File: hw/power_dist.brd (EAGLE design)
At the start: 80 x 50 mm, 72 parts, among them J1 JST-ZH6SMT_VERT, J2 JST-PH4SMT_VERT, J3 JST-PH5VERT, P1 XT30P, P2 XT30P, P3 XT30P, P4 XT30P, P5 XT30P, P6 XT30P, P7 XT90PW-M, Q1 PSMN4R8-100BSEJ, Q2 PSMN4R8-100BSEJ, Q3 PSMN4R8-100BSEJ, Q4 MF-DSC-SOT233-MMBT3904, Q5 MMBT5401 100V, U1 MAX15062AATA+T, U2 STM32G474CEU6, U4 TCAN334G, U5 LT1787HVIMS8PBF

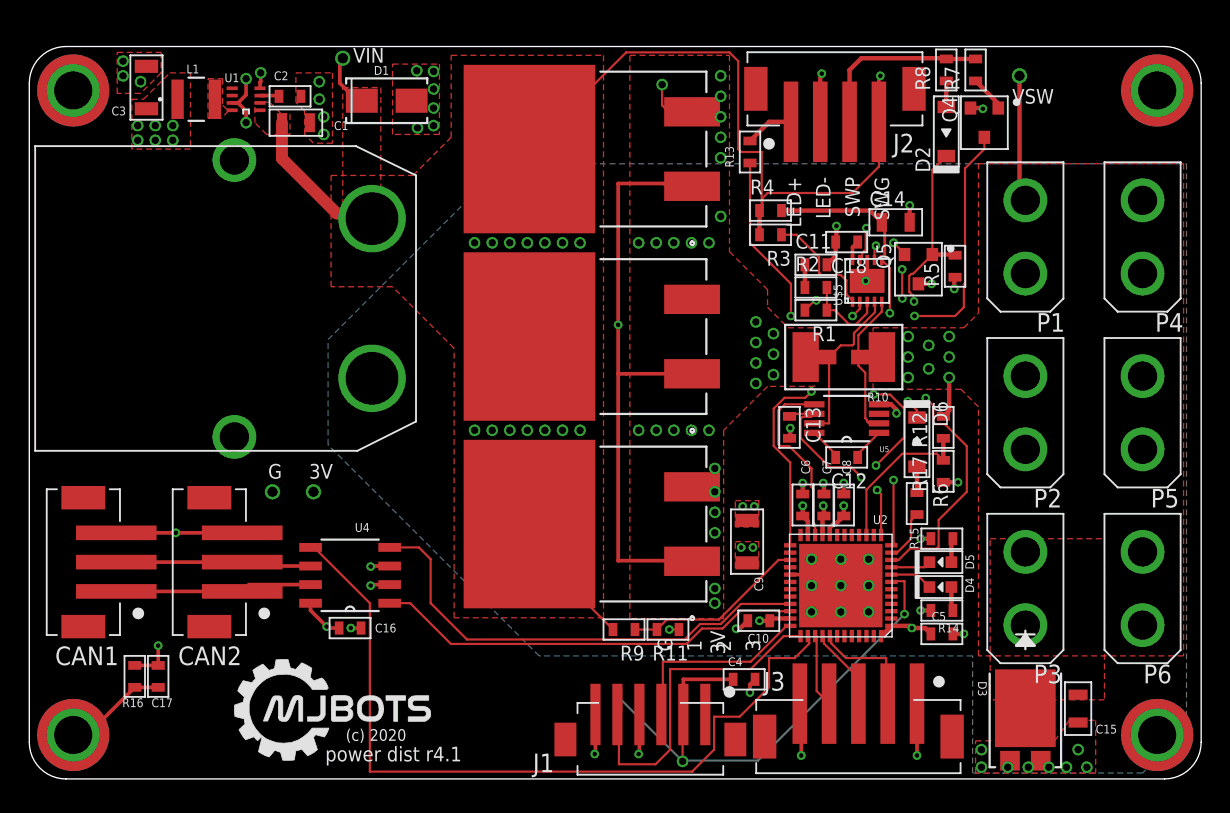
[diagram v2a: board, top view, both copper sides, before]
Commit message: Connect GND/PGND and fix XT90 TH size
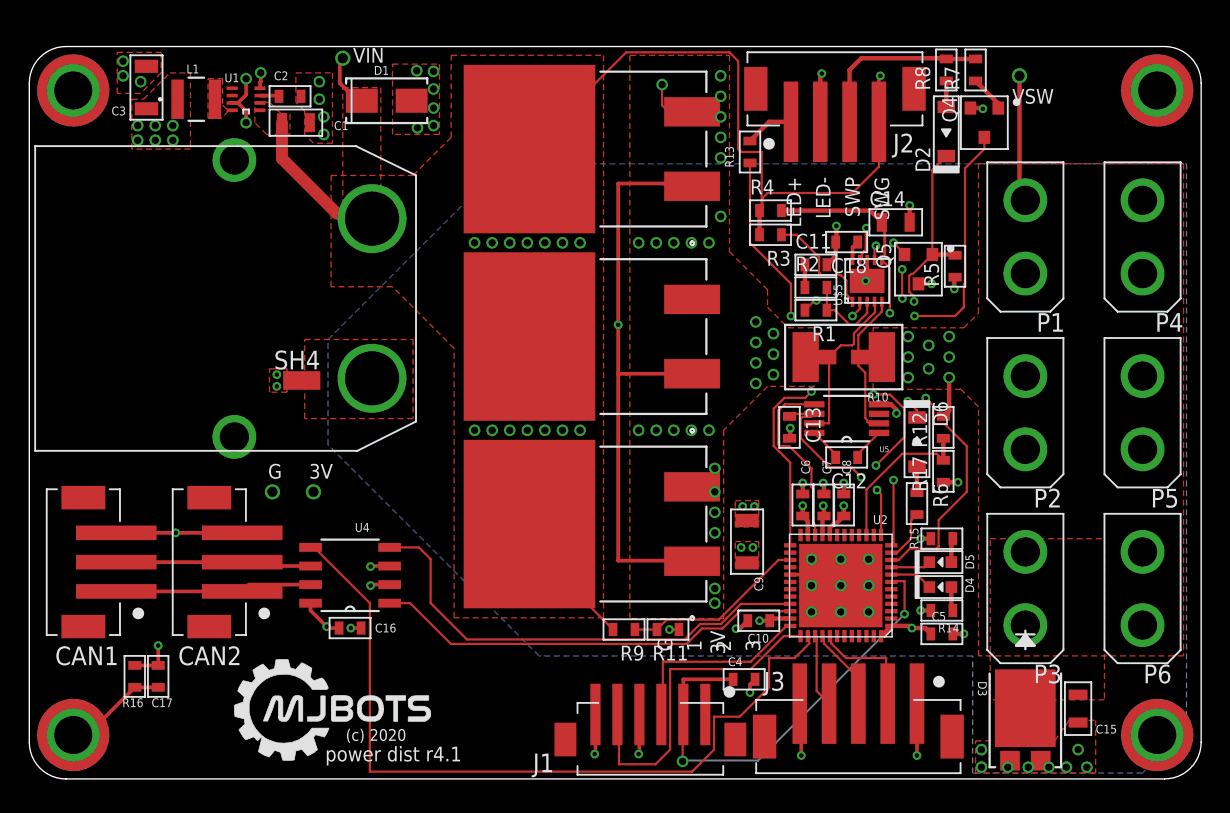
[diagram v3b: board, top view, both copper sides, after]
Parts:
- added SH4: SHORTBIG, shorts:SHORT_TOP-BIG
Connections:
- net GND: now also SH4.1
- net PGND: now also SH4.2
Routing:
- net NRST: track 37.7 -> 31.5 mm
- net GPIO3: track 10.4 -> 7.91 mm
- net SWCLK: track 24.7 -> 22.7 mm
- net GND: vias 49 -> 51
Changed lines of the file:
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@@
 </element>
 <element name="U4" library="precharge" package="SOIC8" value="TCAN334G" x="21.9" y="13.9" smashed="yes" rot="R180">
-<attribute name="MF" value="Analog" x="21.9" y="13.9" size="1.778" layer="27" rot="R180" display="off"/>
-<attribute name="MPN" value="LTC2875IS8" x="21.9" y="13.9" size="1.778" layer="27" rot="R180" display="off"/>
+<attribute name="MF" value="TI" x="21.9" y="13.9" size="1.778" layer="27" rot="R180" display="off"/>
+<attribute name="MPN" value="TCAN334GDR" x="21.9" y="13.9" size="1.778" layer="27" rot="R180" display="off"/>
 <attribute name="NAME" x="22.2234" y="16.865" size="0.6" layer="25" ratio="10" rot="SR0"/>
 <attribute name="POPULATE" value="1" x="21.9" y="13.9" size="1.778" layer="27" rot="R180" display="off"/>
@@
 <attribute name="VOLTAGE" value="" x="62.4" y="21" size="1.778" layer="27" rot="R90" display="off"/>
 <attribute name="WATTAGE" value="" x="62.4" y="21" size="1.778" layer="27" rot="R90" display="off"/>
+</element>
+<element name="SH4" library="shorts" package="SHORT_TOP-BIG" value="SHORTBIG" x="18.6" y="27.2" smashed="yes" rot="R180">
+<attribute name="NAME" x="19.87" y="29.232" size="1.27" layer="25" ratio="16" rot="R180"/>
+<attribute name="POPULATE" value="0" x="18.6" y="26.8" size="1.778" layer="27" rot="R180" display="off"/>
 </element>
 </elements>
@@
 <wire x1="63.15" y1="34.2" x2="63.15" y2="33.45" width="0.3048" layer="1"/>
 <wire x1="60.1" y1="38" x2="60.1" y2="39.15" width="0.3048" layer="1"/>
-<wire x1="57.25" y1="34" x2="57.2" y2="34" width="0.1524" layer="1"/>
 <wire x1="57.2" y1="34" x2="57.1" y2="34" width="0.1524" layer="1"/>
+<contactref element="SH4" pad="1"/>
+<via x="16.9" y="27.6" extent="1-16" drill="0.3048"/>
+<via x="16.9" y="26.8" extent="1-16" drill="0.3048"/>
+<polygon width="0.1524" layer="1" thermals="no">
+<vertex x="16.6" y="28"/>
+<vertex x="17.6" y="28"/>
+<vertex x="17.6" y="26.4"/>
+<vertex x="16.4" y="26.4"/>
+<vertex x="16.4" y="28"/>
+</polygon>
 </signal>
 <signal name="VCC" class="1">
@@
 <wire x1="48.05" y1="6.8" x2="44.65" y2="6.8" width="0.254" layer="1"/>
 <wire x1="44.65" y1="6.8" x2="44.65" y2="4.4" width="0.254" layer="1"/>
-<wire x1="58.85" y1="13.45" x2="58.9" y2="13.4" width="0.1524" layer="1"/>
-<wire x1="44.6" y1="1.2" x2="40.4" y2="5.4" width="0.1524" layer="16"/>
-<wire x1="40.4" y1="5.4" x2="40.2" y2="5.4" width="0.1524" layer="16"/>
 <via x="44.6" y="1.2" extent="1-16" drill="0.5"/>
 <wire x1="44.6" y1="1.2" x2="44.6" y2="4.35" width="0.1524" layer="1"/>
@@
 <contactref element="J1" pad="5"/>
 <contactref element="U2" pad="37"/>
-<wire x1="40.4" y1="4.65" x2="40.15" y2="4.4" width="0.1524" layer="1"/>
-<wire x1="40.4" y1="6.2" x2="40.4" y2="4.65" width="0.1524" layer="1"/>
 <wire x1="51.5" y1="9.75" x2="52.65" y2="9.75" width="0.1524" layer="1"/>
 <wire x1="49.25" y1="7.5" x2="51.5" y2="9.75" width="0.1524" layer="1"/>
@@
 <wire x1="40.25" y1="1" x2="42.75" y2="1" width="0.1524" layer="1"/>
 <wire x1="40.25" y1="4.25" x2="40.25" y2="1" width="0.1524" layer="1"/>
-<wire x1="52.75" y1="9.75" x2="52.65" y2="9.75" width="0.1524" layer="1"/>
 <wire x1="40.25" y1="4.25" x2="40.15" y2="4.4" width="0.1524" layer="1"/>
 </signal>
@@
 <contactref element="J3" pad="2"/>
 <contactref element="U2" pad="41"/>
-<wire x1="58.6" y1="7.6" x2="58.6" y2="5.14" width="0.1524" layer="1"/>
 <wire x1="54.75" y1="9.25" x2="54.75" y2="9.75" width="0.1524" layer="1"/>
 <wire x1="55.75" y1="8.25" x2="54.75" y2="9.25" width="0.1524" layer="1"/>
@@
 <via x="72.2" y="0.8" extent="1-16" drill="0.5"/>
 <via x="71.6" y="2" extent="1-16" drill="0.5"/>
+<polygon width="0.1524" layer="1" thermals="no">
+<vertex x="18.8" y="30"/>
+<vertex x="26.2" y="30"/>
+<vertex x="26.2" y="24.6"/>
+<vertex x="18.8" y="24.6"/>
+</polygon>
+<contactref element="SH4" pad="2"/>
 </signal>
 </signals>

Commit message: Resize and draft place all silks
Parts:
- added C19, C20: 0.01uF, mfpassives:C0603
- added D7, D8: MF-DIO-SOD123-1N4148, mfdiscretesemi:SOD-123
- added R18: DNP, mfpassives:R0603
- moved DB_VIN 1.56 mm to (22.4, 48.0)
- moved R3 0.80 mm to (51.4, 37.1)
- moved R4 0.80 mm to (51.4, 38.8)
- moved C2 0.40 mm to (17.8, 47.0)
- moved C9 0.15 mm to (48.9, 16.2)
- renumbered U$5 to U6
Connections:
- new net 3V3_EN: D7.CATHODE, D8.CATHODE, R18.P$2, U1.2
- new net 3V3_OVERRIDE: D8.ANODE, U2.26
- net +24V: no longer U1.2
- net GND: now also C19.P$2, C20.P$2, R18.P$1
- net VIN_POST: now also D7.ANODE
- net VIN_SAMP: now also C20.P$1
- net VSWITCHED_SAMP: now also C19.P$1
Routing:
- net 3V3_EN: track 0.00 -> 71.0 mm, vias 0 -> 4
- net 3V3_OVERRIDE: track 0.00 -> 7.02 mm
- net GND: track 48.4 -> 51.3 mm, vias 51 -> 54
- net VIN_POST: track 4.64 -> 2.21 mm, vias 30 -> 29
- net +24V: track 70.3 -> 69.0 mm
- net VIN_SAMP: track 12.6 -> 13.8 mm
- net LTC_VCC: track 17.7 -> 16.9 mm
- net N$10: track 7.96 -> 7.16 mm
- net FLT: track 25.3 -> 26.1 mm
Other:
- board text added: "L+"
- board text added: "L-"
- board text added: "SG"
- board text added: "SP"
- board text removed: "LED+"
- board text removed: "LED-"
- board text removed: "SWG"
- board text removed: "SWP"

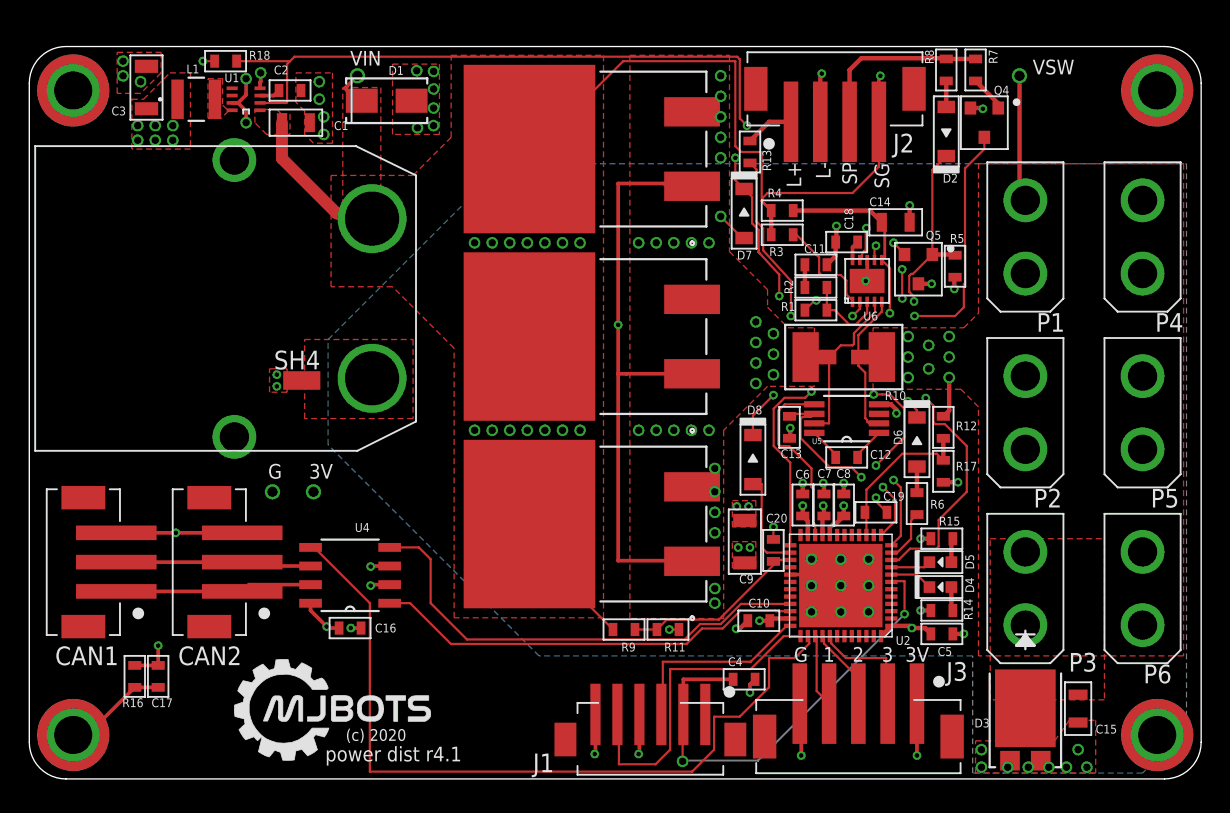
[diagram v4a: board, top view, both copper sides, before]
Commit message: Rename all resistors, capacitors, and diodes
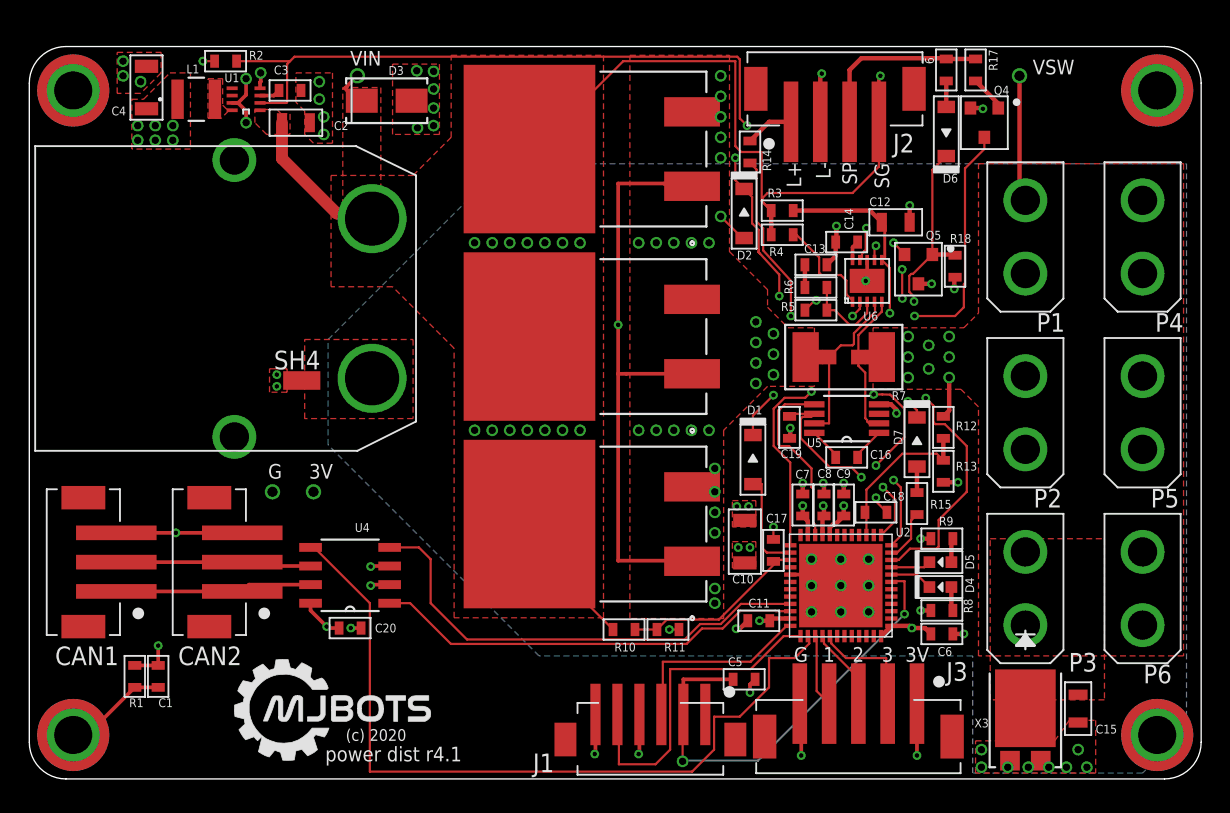
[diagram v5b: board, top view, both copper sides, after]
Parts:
- removed D8: MF-DIO-SOD123-1N4148, mfdiscretesemi:SOD-123
- removed R16: DNP, mfpassives:R0603
- added !6: 500k, mfpassives:R0603
- added X3: FSV10150VTO277-3L_ONS-L, power_dist:TO277-3L_ONS-L
- C1: value 1uF 100V -> DNP; device mfpassives:C0805 -> mfpassives:C0603
- C10, C4: value 0.1uF -> 10uF 50V; device mfpassives:C0603 -> mfpassives:C1206
- C11: value (none) -> 0.1uF
- C12: value DNP -> 1uF 100V; device mfpassives:C0603 -> mfpassives:C0805
- C13: value 0.1uF -> (none)
- C14: value 1uF 100V -> 0.1uF; device mfpassives:C0805 -> mfpassives:C0603
- C16: value 0.1uF -> DNP
- C17: value DNP -> 0.01uF
- C18: value 0.1uF -> 0.01uF
- C19, C20: value 0.01uF -> 0.1uF
- C2: value 1uF -> 1uF 100V; device mfpassives:C0603 -> mfpassives:C0805
- C3: value 10uF 50V -> 1uF; device mfpassives:C1206 -> mfpassives:C0603
- C6: value 1uF -> 0.1uF
- C7: value 0.1uF -> 1uF
- C9: value 10uF 50V -> 0.1uF; device mfpassives:C1206 -> mfpassives:C0603
- D1: value SMBJ51CA-E3/52 -> MF-DIO-SOD123-1N4148; device power_dist:DIODE_DO-214AC -> mfdiscretesemi:SOD-123
- D3: value FSV10150VTO277-3L_ONS-L -> SMBJ51CA-E3/52; device power_dist:TO277-3L_ONS-L -> power_dist:DIODE_DO-214AC
- R1, R2: value (none) -> DNP
- R10: value 0.5mOhm -> 3M 1%; device power_dist:SHUNT2512 -> mfpassives:R0603
- R13: value 220 -> 200k 1%
- R15: value 220 -> 1k
- R17: value 200k 1% -> 2M
- R18: value DNP -> 200k
- R3: value (none) -> 10k
- R4: value 10k -> (none)
- R5: value 200k -> (none)
- R6: value 1k -> (none)
- R7: value 2M -> 0.5mOhm; device mfpassives:R0603 -> power_dist:SHUNT2512
- R8: value 500k -> 220
- R9: value 3M 1% -> 220
- moved D3 60.7 mm to (24.4, 46.3)
- moved C4 57.4 mm to (8.00, 47.2), turned to 90 degrees
- moved R1 52.8 mm to (7.20, 7.00), turned to 90 degrees
- moved R18 51.7 mm to (63.2, 35.0), turned to 90 degrees
- moved R2 43.2 mm to (13.4, 49.0)
- moved C17 42.9 mm to (50.8, 15.6)
- moved C1 39.0 mm to (8.80, 7.00), turned to 90 degrees
- moved R8 36.9 mm to (62.3, 11.5), turned to 180 degrees
- moved C16 35.8 mm to (55.8, 21.9)
- moved D1 35.0 mm to (49.4, 21.8), turned to 270 degrees
- moved R14 33.9 mm to (49.2, 42.8), turned to 270 degrees
- moved C20 29.4 mm to (21.9, 10.3), turned to 180 degrees
- moved R17 27.5 mm to (64.6, 48.4)
- moved R13 25.5 mm to (62.4, 21.0), turned to 90 degrees
- moved C11 24.6 mm to (49.8, 10.8), turned to 180 degrees
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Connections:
- net +24V: now also C2.P$1, D3.1, R10.P$2, R3.P$1, R4.P$2; no longer C1.P$1, D1.1, R3.P$2, R4.P$1, R9.P$2
- net 3V3_EN: now also D1.CATHODE, D2.CATHODE, R2.P$2; no longer D7.CATHODE, D8.CATHODE, R18.P$2
- net 3V3_OVERRIDE: now also D1.ANODE; no longer D8.ANODE
- net GATE: now also R5.P$2; no longer R1.P$2
- net GND: now also C12.P$2, D3.2, R1.P$2, R13.P$1, R2.P$1; no longer C16.P$2, D1.2, R16.P$2, R17.P$1, R5.P$1
- net ISAMP_BIAS: now also C19.P$1; no longer C13.P$1
- net LTC_VCC: now also C12.P$1, R3.P$2; no longer C14.P$1, R4.P$2
- net N$10: now also R4.P$1; no longer R3.P$1
- net N$11: now also R17.P$1; no longer R7.P$1
- net N$12: now also C14.P$1; no longer C18.P$1
- net N$13: now also D7.CATHODE, R18.P$2; no longer D2.CATHODE, R5.P$2
- net N$14: now also R9.P$1; no longer R15.P$1
- net N$15: now also C1.P$1, R1.P$1; no longer C17.P$1, R16.P$1
- net N$17: now also !6.P$1, D6.ANODE; no longer D2.ANODE, R8.P$1
- net N$18: now also D7.ANODE, R15.P$1; no longer D6.ANODE, R6.P$1
- net N$2: now also R14.P$1; no longer R13.P$1
- net N$4: now also C3.P$1; no longer C2.P$1
- net N$5: now also R5.P$1, R6.P$2; no longer R1.P$1, R2.P$2
- net N$6: now also C16.P$1; no longer C12.P$1
- net N$7: now also C16.P$2; no longer C12.P$2
- net N$8: now also R8.P$1; no longer R14.P$1
- net N$9: now also C13.P$1, R6.P$1; no longer C11.P$1, R2.P$1
- net NRST: now also C5.P$1; no longer C4.P$1
- net PGND: now also X3.1, X3.2; no longer D3.1, D3.2
- net PWR_LED: now also R14.P$2; no longer R13.P$2
- net PWR_OVERRIDE: now also R15.P$2; no longer R6.P$2
- net PWR_SW: now also !6.P$2, R17.P$2; no longer R7.P$2, R8.P$2
- net VCC: now also C11.P$1, C20.P$1, C4.P$1, R8.P$2, R9.P$2; no longer C16.P$1, C3.P$1, C5.P$1, R14.P$2, R15.P$2
- net VIN_POST: now also D2.ANODE, R7.1; no longer D7.ANODE, R10.1
- net VIN_SAMP: now also C17.P$1, R10.P$1; no longer C20.P$1, R9.P$1
- net VSENSE_HIGH: now also R7.3; no longer R10.3
- net VSENSE_LOW: now also R7.4; no longer R10.4
- net VSWITCHED: now also R7.2, X3.3; no longer D3.3, R10.2
- net VSWITCHED_SAMP: now also C18.P$1, R13.P$2; no longer C19.P$1, R17.P$2
